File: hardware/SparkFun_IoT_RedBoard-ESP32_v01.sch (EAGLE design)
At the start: 114 parts, among them J1 5.5x2.1mm Barrel, J13 QWIIC_RIGHT_ANGLE, J15 MICRO-SD-PUSH-PUSH-EXT-PIN, J2 USB C, J3 USB_SOLDER_PADS, J5 M10NO_SILK, Q1 MBT3904DW1T1, Q11 20V/4.2A/52mΩ/1.4W, Q13 20V/4.2A/52mΩ/1.4W, Q3 20V/4.2A/52mΩ/1.4W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

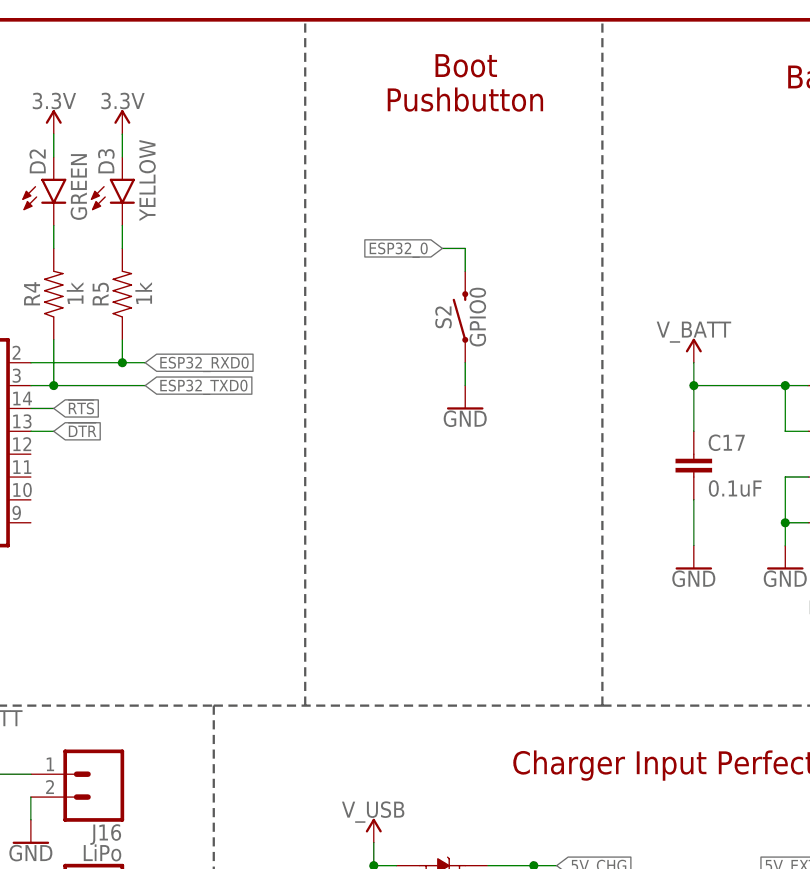
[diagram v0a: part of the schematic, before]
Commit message: Add addressable status LED
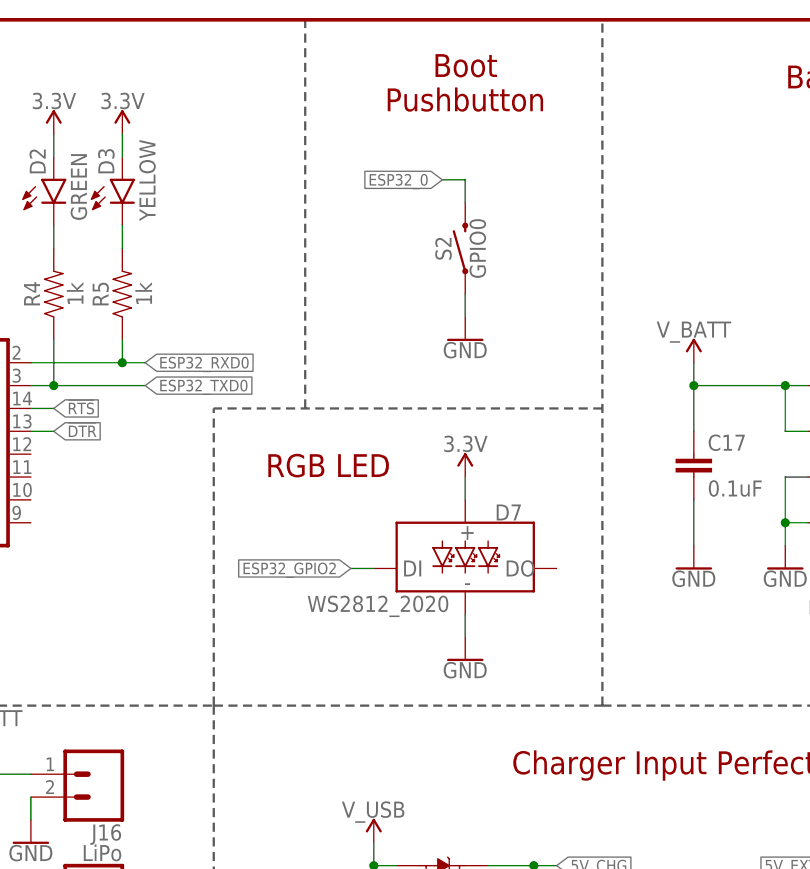
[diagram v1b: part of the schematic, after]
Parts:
- added D7: WS2812_2020, SparkFun-LED:WS2812_2020
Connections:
- net 3.3V: now also D7.VCC
- net ESP32_GPIO2: now also D7.DI
- net GND: now also D7.GND
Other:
- note added: "RGB LED"
- moved on the sheet: S2
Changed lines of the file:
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@@
 <part name="C18" library="SparkFun-Capacitors" deviceset="0.1UF" device="-0603-25V-(+80/-20%)" value="0.1uF"/>
 <part name="GND54" library="SparkFun-PowerSymbols" deviceset="GND" device=""/>
+<part name="D7" library="SparkFun-LED" deviceset="WS2812" device="_2020"/>
+<part name="GND55" library="SparkFun-PowerSymbols" deviceset="GND" device=""/>
+<part name="SUPPLY29" library="SparkFun-PowerSymbols" deviceset="3.3V" device=""/>
 </parts>
 <sheets>
@@
 <text x="403.86" y="40.64" size="1.27" layer="97" font="vector" align="bottom-center">Open jumper to remove I2C pullups.</text>
 <text x="331.47" y="6.604" size="2.54" layer="94" font="vector">Revised by: Dryw Wade</text>
-<wire x1="327.66" y1="203.2" x2="327.66" y2="279.4" width="0.254" layer="97" style="longdash"/>
 <text x="176.022" y="7.874" size="1.778" layer="96" font="vector" ratio="9">25V</text>
+<wire x1="327.66" y1="236.22" x2="327.66" y2="279.4" width="0.254" layer="97" style="longdash"/>
+<wire x1="360.68" y1="236.22" x2="317.5" y2="236.22" width="0.254" layer="97" style="longdash"/>
+<wire x1="317.5" y1="203.2" x2="317.5" y2="236.22" width="0.254" layer="97" style="longdash"/>
+<text x="330.2" y="228.6" size="2.54" layer="94" font="vector" ratio="11" align="bottom-center">RGB LED</text>
 </plain>
 <instances>
@@
 <attribute name="VALUE" x="25.4" y="193.294" size="1.778" layer="96" align="bottom-center"/>
 </instance>
-<instance part="S2" gate="G$1" x="345.44" y="246.38" smashed="yes" rot="R90">
-<attribute name="NAME" x="343.916" y="246.38" size="1.778" layer="95" font="vector" rot="R90" align="bottom-center"/>
-<attribute name="VALUE" x="345.948" y="246.38" size="1.778" layer="96" font="vector" rot="R90" align="top-center"/>
+<instance part="S2" gate="G$1" x="345.44" y="254" smashed="yes" rot="R90">
+<attribute name="NAME" x="343.916" y="254" size="1.778" layer="95" font="vector" rot="R90" align="bottom-center"/>
+<attribute name="VALUE" x="345.948" y="254" size="1.778" layer="96" font="vector" rot="R90" align="top-center"/>
 </instance>
 <instance part="D2" gate="G$1" x="299.72" y="261.62" smashed="yes">
@@
 <attribute name="VALUE" x="342.9" y="48.006" size="1.778" layer="96" align="top-center"/>
 </instance>
-<instance part="GND23" gate="1" x="345.44" y="236.22" smashed="yes">
-<attribute name="VALUE" x="345.44" y="235.966" size="1.778" layer="96" align="top-center"/>
+<instance part="GND23" gate="1" x="345.44" y="243.84" smashed="yes">
+<attribute name="VALUE" x="345.44" y="243.586" size="1.778" layer="96" align="top-center"/>
 </instance>
 <instance part="GND35" gate="1" x="231.14" y="5.08" smashed="yes">
@@
 <instance part="GND54" gate="1" x="175.26" y="5.08" smashed="yes">
 <attribute name="VALUE" x="175.26" y="4.826" size="1.778" layer="96" align="top-center"/>
+</instance>
+<instance part="D7" gate="G$1" x="345.44" y="218.44" smashed="yes">
+<attribute name="NAME" x="350.266" y="223.774" size="1.778" layer="95" font="vector" align="bottom-center"/>
+<attribute name="VALUE" x="335.788" y="213.614" size="1.778" layer="96" font="vector" align="bottom-center"/>
+</instance>
+<instance part="GND55" gate="1" x="345.44" y="208.28" smashed="yes">
+<attribute name="VALUE" x="345.44" y="208.026" size="1.778" layer="96" align="top-center"/>
+</instance>
+<instance part="SUPPLY29" gate="G$1" x="345.44" y="228.6" smashed="yes">
+<attribute name="VALUE" x="345.44" y="231.394" size="1.778" layer="96" align="bottom-center"/>
 </instance>
 </instances>
@@
 </segment>
 <segment>
-<wire x1="345.44" y1="241.3" x2="345.44" y2="238.76" width="0.1524" layer="91"/>
+<wire x1="345.44" y1="248.92" x2="345.44" y2="246.38" width="0.1524" layer="91"/>
 <pinref part="S2" gate="G$1" pin="1"/>
 <pinref part="GND23" gate="1" pin="GND"/>
@@
 <pinref part="GND54" gate="1" pin="GND"/>
 </segment>
+<segment>
+<pinref part="D7" gate="G$1" pin="GND"/>
+<wire x1="345.44" y1="213.36" x2="345.44" y2="210.82" width="0.1524" layer="91"/>
+<pinref part="GND55" gate="1" pin="GND"/>
+</segment>
 </net>
 <net name="VIN" class="1">
@@
 <wire x1="340.36" y1="124.46" x2="340.36" y2="121.92" width="0.1524" layer="91"/>
 </segment>
+<segment>
+<pinref part="D7" gate="G$1" pin="VCC"/>
+<wire x1="345.44" y1="226.06" x2="345.44" y2="228.6" width="0.1524" layer="91"/>
+<pinref part="SUPPLY29" gate="G$1" pin="3.3V"/>
+</segment>
 </net>
 <net name="ESP32_SCL" class="0">
@@
 <segment>
 <pinref part="S2" gate="G$1" pin="2"/>
-<wire x1="345.44" y1="251.46" x2="345.44" y2="254" width="0.1524" layer="91"/>
-<label x="342.9" y="254" size="1.27" layer="95" rot="R180" xref="yes"/>
-<wire x1="342.9" y1="254" x2="345.44" y2="254" width="0.1524" layer="91"/>
+<wire x1="345.44" y1="259.08" x2="345.44" y2="261.62" width="0.1524" layer="91"/>
+<label x="342.9" y="261.62" size="1.27" layer="95" rot="R180" xref="yes"/>
+<wire x1="342.9" y1="261.62" x2="345.44" y2="261.62" width="0.1524" layer="91"/>
 </segment>
 <segment>
@@
 <label x="76.2" y="238.76" size="1.27" layer="95" xref="yes"/>
 </segment>
-</net>
+<segment>
+<pinref part="D7" gate="G$1" pin="DI"/>
+<wire x1="335.28" y1="218.44" x2="332.74" y2="218.44" width="0.1524" layer="91"/>
+<label x="332.74" y="218.44" size="1.27" layer="95" rot="R180" xref="yes"/>
+</segment>
+</net>
